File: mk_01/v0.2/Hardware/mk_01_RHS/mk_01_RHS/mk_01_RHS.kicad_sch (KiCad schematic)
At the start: 90 parts, among them SW1 SW_Push_Dual, U1 nice_nano

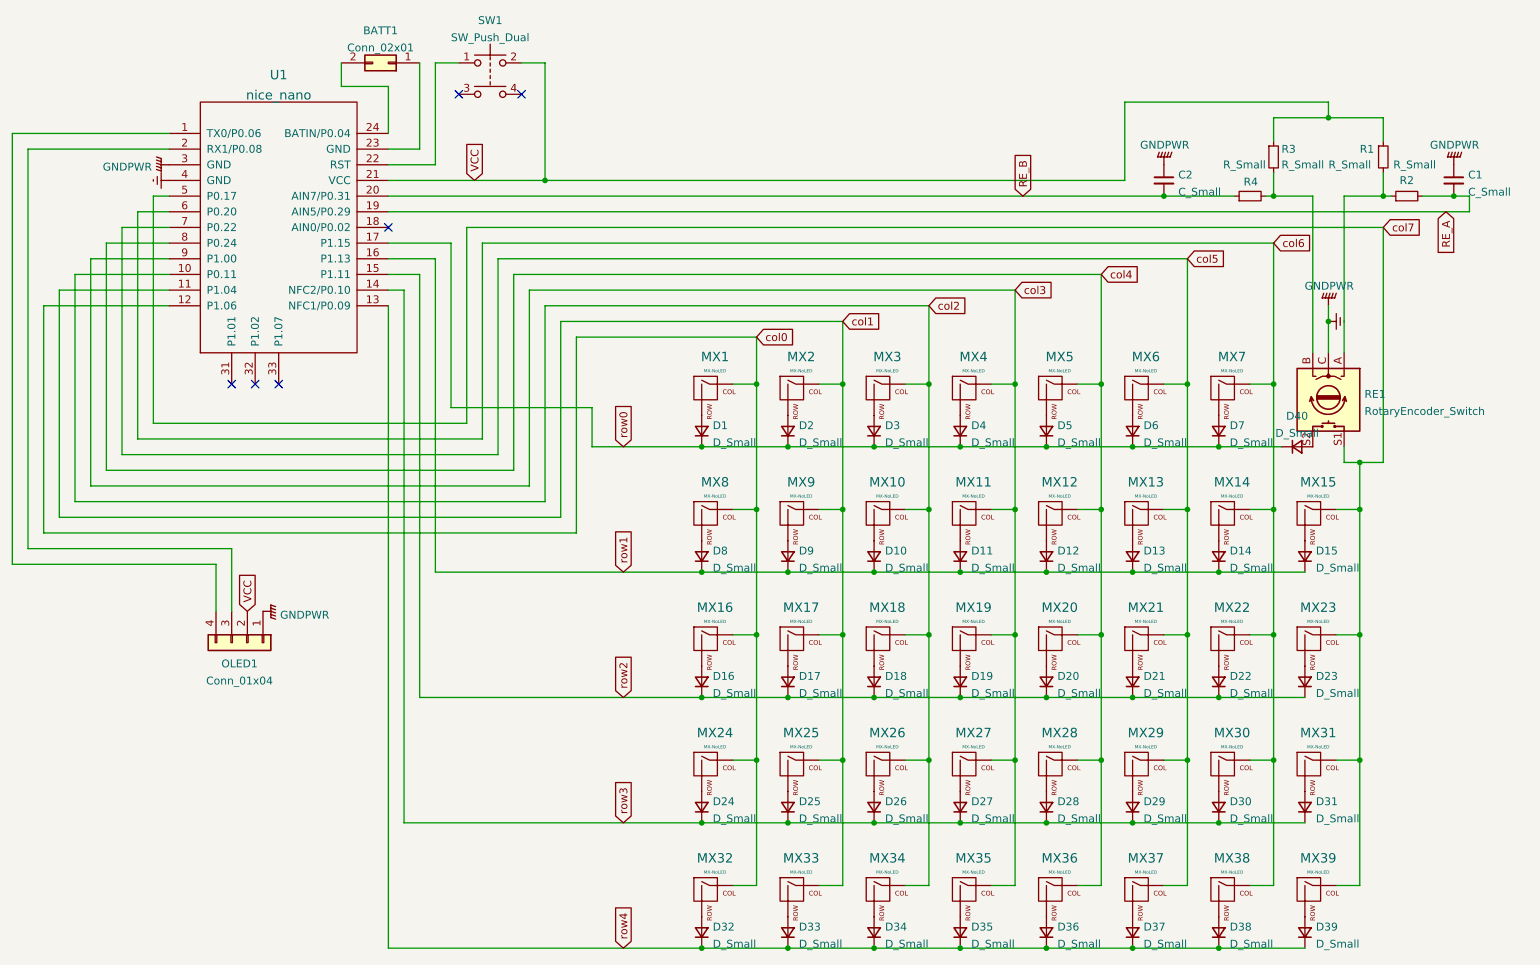
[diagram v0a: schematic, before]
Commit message: Right hand side mostly completed
The right hand side of the keyboard is pretty much complete, and after a final checkover of everything I think it's ready for production. I'm going to clean up the left hand side board design and schematic to match the right hand schematic style, since I based the left hand side on v0.1, and the right hand side was done from scratch.
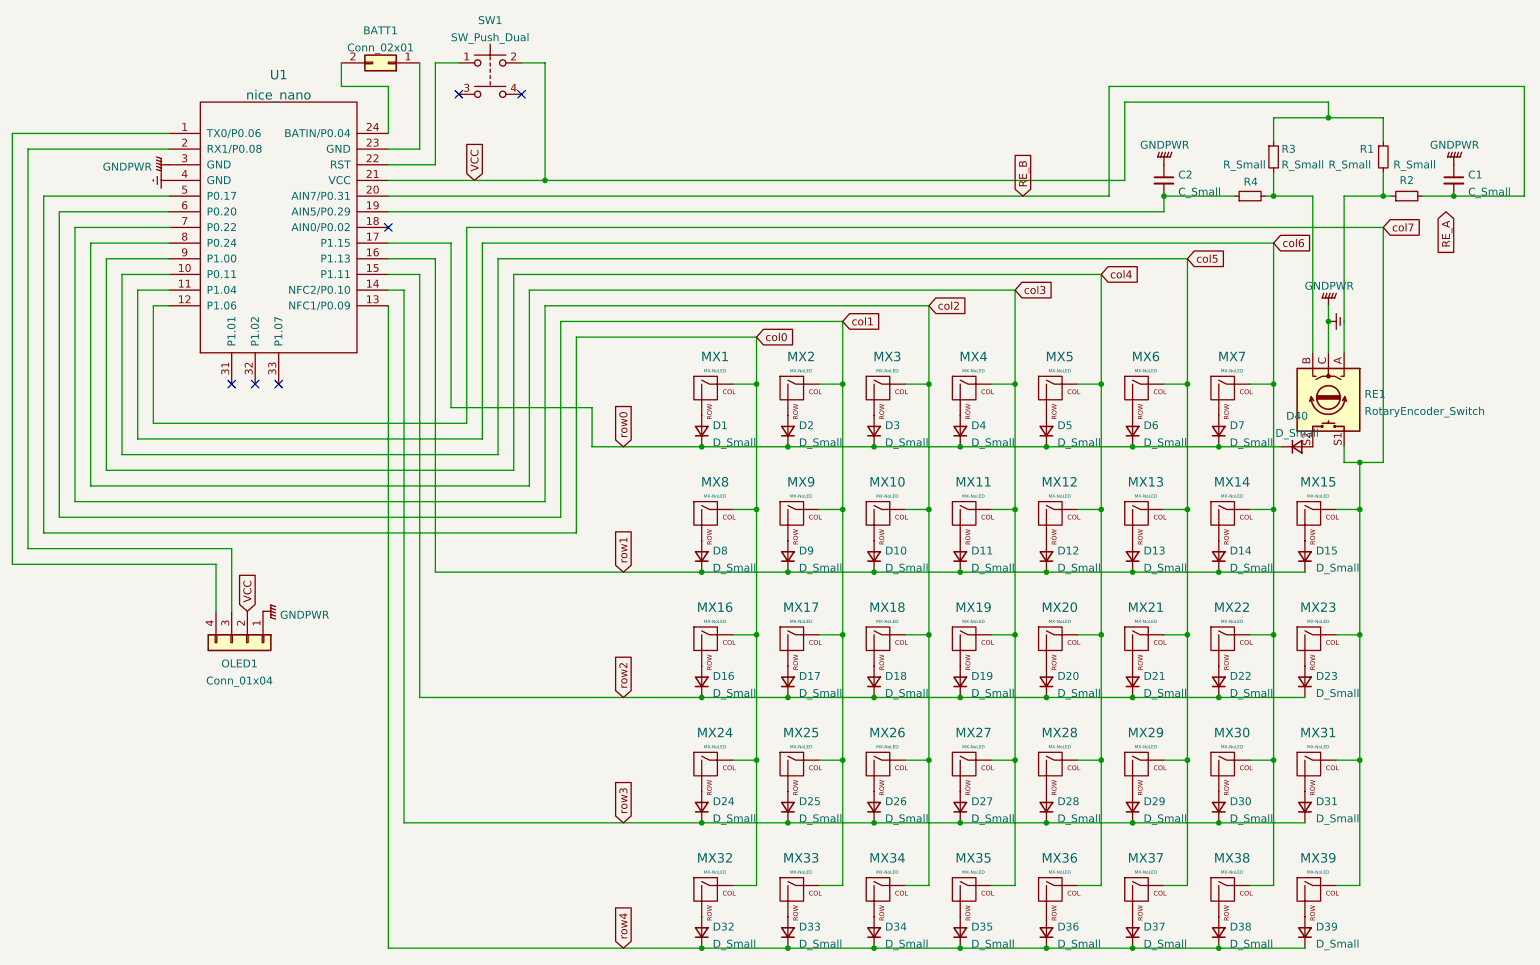
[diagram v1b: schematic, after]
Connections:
- net RE_A: no longer C1.2, R2.2, U1.19 (AIN5/P0.29)
- net RE_B: now also C1.2, R2.2; no longer C2.2, R4.1
- net col0: now also U1.5 (P0.17); no longer U1.12 (P1.06)
- net col1: now also U1.6 (P0.20); no longer U1.11 (P1.04)
- net col2: now also U1.7 (P0.22); no longer U1.10 (P0.11)
- net col3: now also U1.8 (P0.24); no longer U1.9 (P1.00)
- net col4: now also U1.9 (P1.00); no longer U1.8 (P0.24)
- net col5: now also U1.10 (P0.11); no longer U1.7 (P0.22)
- net col6: now also U1.11 (P1.04); no longer U1.6 (P0.20)
- net col7: now also U1.12 (P1.06); no longer U1.5 (P0.17)
- new net: C2.2, R4.1, U1.19 (AIN5/P0.29)
